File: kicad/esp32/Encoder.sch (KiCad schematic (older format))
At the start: 3 parts, among them P13 ENC_Host, P14 ENC_Slave, U11 AS5145

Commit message: 自動配線成功
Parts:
- renumbered P13 to P12, P14 to P13
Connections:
- net +3V3: now also P12.1 (P1); no longer P12.4 (P4)
- net CSn: now also P12.5 (P5); no longer P12.3 (P3)
- net GND: now also P12.6 (P6); no longer P12.5 (P5)
- net MISO: now also P12.4 (P4); no longer P12.1 (P1)
- net MOSI: now also P12.3 (P3); no longer P12.6 (P6)
- net s_3.3V: now also P13.1 (P1); no longer P13.4 (P4)
- net s_CSn: now also P13.5 (P5); no longer P13.3 (P3)
- net s_MISO: now also P13.4 (P4); no longer P13.1 (P1)
- net s_MOSI: now also P13.3 (P3); no longer P13.6 (P6)
- net s_VSS: now also P13.6 (P6); no longer P13.5 (P5)
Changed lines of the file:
@@
 $Descr A4 11693 8268
 encoding utf-8
-Sheet 10 13
+Sheet 10 14
 Title ""
 Date ""
@@
 $EndComp
 $Comp
-L CONN_01X06 P14
+L CONN_01X06 P13
 U 1 1 589E8902
 P 5800 2350
-AR Path="/589E8312/589E8902" Ref="P14"  Part="1"
-AR Path="/589F1140/589E8902" Ref="P16"  Part="1"
-F 0 "P14" H 5800 2700 50  0000 C CNN
+AR Path="/589E8312/589E8902" Ref="P13"  Part="1"
+AR Path="/589F1140/589E8902" Ref="P15"  Part="1"
+F 0 "P13" H 5800 2700 50  0000 C CNN
 F 1 "ENC_Slave" V 5900 2350 50  0000 C CNN
 F 2 "mouse:STAND_AS_SLAVE" H 5800 2350 50  0001 C CNN
@@
 	-1   0    0    -1
 $EndComp
+Text Label 6100 2100 0    60   ~ 0
+s_3.3V
+Text Label 6100 2600 0    60   ~ 0
+s_VSS
+Text Label 6100 2300 0    60   ~ 0
+s_MOSI
 Text Label 6100 2400 0    60   ~ 0
-s_3.3V
+s_MISO
 Text Label 6100 2500 0    60   ~ 0
-s_VSS
-Text Label 6100 2600 0    60   ~ 0
-s_MOSI
-Text Label 6100 2100 0    60   ~ 0
-s_MISO
-Text Label 6100 2300 0    60   ~ 0
 s_CSn
 Text Label 6100 2200 0    60   ~ 0
@@
 NoConn ~ 4900 3700
 Wire Wire Line
-	6000 2400 6700 2400
+	6000 2100 6700 2100
 Wire Wire Line
-	6000 2500 6700 2500
+	6000 2600 6700 2600
+Wire Wire Line
+	6100 2300 6000 2300
+Wire Wire Line
+	6000 2500 6100 2500
 Wire Wire Line
 	6100 2200 6000 2200
 Wire Wire Line
-	6000 2600 6100 2600
-Wire Wire Line
-	6100 2100 6000 2100
-Wire Wire Line
-	6000 2300 6100 2300
+	6000 2400 6100 2400
 Text Label 6400 3200 0    60   ~ 0
 s_3.3V
@@
 	6400 3700 6300 3700
 $Comp
-L CONN_01X06 P13
+L CONN_01X06 P12
 U 1 1 589E9420
 P 5400 2350
-AR Path="/589E8312/589E9420" Ref="P13"  Part="1"
-AR Path="/589F1140/589E9420" Ref="P15"  Part="1"
-F 0 "P13" H 5400 2700 50  0000 C CNN
+AR Path="/589E8312/589E9420" Ref="P12"  Part="1"
+AR Path="/589F1140/589E9420" Ref="P14"  Part="1"
+F 0 "P12" H 5400 2700 50  0000 C CNN
 F 1 "ENC_Host" V 5500 2350 50  0000 C CNN
 F 2 "mouse:STAND_AS_HOST" H 5400 2350 50  0001 C CNN
@@
 $EndComp
 $Comp
-L GND #PWR059
+L GND #PWR056
 U 1 1 589E94E9
 P 5100 2700
-AR Path="/589E8312/589E94E9" Ref="#PWR059"  Part="1"
-AR Path="/589F1140/589E94E9" Ref="#PWR063"  Part="1"
-F 0 "#PWR063" H 5100 2450 50  0001 C CNN
+AR Path="/589E8312/589E94E9" Ref="#PWR056"  Part="1"
+AR Path="/589F1140/589E94E9" Ref="#PWR060"  Part="1"
+F 0 "#PWR060" H 5100 2450 50  0001 C CNN
 F 1 "GND" H 5100 2550 50  0000 C CNN
 F 2 "" H 5100 2700 50  0000 C CNN
@@
 Text HLabel 5000 2200 0    60   Input ~ 0
 SCLK
-Text HLabel 5000 2600 0    60   Input ~ 0
+Text HLabel 5000 2300 0    60   Input ~ 0
 MOSI
-Text HLabel 5000 2100 0    60   Input ~ 0
+Text HLabel 5000 2400 0    60   Input ~ 0
 MISO
-Text HLabel 5000 2300 0    60   Input ~ 0
+Text HLabel 5000 2500 0    60   Input ~ 0
 CSn
+Wire Wire Line
+	5000 2300 5200 2300
 Wire Wire Line
 	5000 2200 5200 2200
 Wire Wire Line
-	5000 2100 5200 2100
-Wire Wire Line
-	5200 2300 5000 2300
+	5200 2400 5000 2400
 $Comp
-L PWR_FLAG #FLG060
+L PWR_FLAG #FLG057
 U 1 1 58CB39A3
-P 6700 2400
-AR Path="/589E8312/58CB39A3" Ref="#FLG060"  Part="1"
-AR Path="/589F1140/58CB39A3" Ref="#FLG064"  Part="1"
-F 0 "#FLG064" H 6700 2495 50  0001 C CNN
-F 1 "PWR_FLAG" H 6700 2580 50  0000 C CNN
-F 2 "" H 6700 2400 50  0000 C CNN
-F 3 "" H 6700 2400 50  0000 C CNN
-	1    6700 2400
+P 6700 2100
+AR Path="/589E8312/58CB39A3" Ref="#FLG057"  Part="1"
+AR Path="/589F1140/58CB39A3" Ref="#FLG061"  Part="1"
+F 0 "#FLG061" H 6700 2195 50  0001 C CNN
+F 1 "PWR_FLAG" H 6700 2280 50  0000 C CNN
+F 2 "" H 6700 2100 50  0000 C CNN
+F 3 "" H 6700 2100 50  0000 C CNN
+	1    6700 2100
 	1    0    0    -1
 $EndComp
 $Comp
-L PWR_FLAG #FLG061
+L PWR_FLAG #FLG058
 U 1 1 58CB39EE
-P 6700 2500
-AR Path="/589E8312/58CB39EE" Ref="#FLG061"  Part="1"
-AR Path="/589F1140/58CB39EE" Ref="#FLG065"  Part="1"
-F 0 "#FLG065" H 6700 2595 50  0001 C CNN
-F 1 "PWR_FLAG" H 6700 2680 50  0000 C CNN
-F 2 "" H 6700 2500 50  0000 C CNN
-F 3 "" H 6700 2500 50  0000 C CNN
-	1    6700 2500
+P 6700 2600
+AR Path="/589E8312/58CB39EE" Ref="#FLG058"  Part="1"
+AR Path="/589F1140/58CB39EE" Ref="#FLG062"  Part="1"
+F 0 "#FLG062" H 6700 2695 50  0001 C CNN
+F 1 "PWR_FLAG" H 6700 2780 50  0000 C CNN
+F 2 "" H 6700 2600 50  0000 C CNN
+F 3 "" H 6700 2600 50  0000 C CNN
+	1    6700 2600
 	-1   0    0    1
 $EndComp
@@
 	6400 3300 6300 3300
 $Comp
-L +3.3V #PWR062
+L +3.3V #PWR059
 U 1 1 589CCACF
 P 5100 2000
-AR Path="/589E8312/589CCACF" Ref="#PWR062"  Part="1"
-AR Path="/589F1140/589CCACF" Ref="#PWR066"  Part="1"
-F 0 "#PWR066" H 5100 1850 50  0001 C CNN
+AR Path="/589E8312/589CCACF" Ref="#PWR059"  Part="1"
+AR Path="/589F1140/589CCACF" Ref="#PWR063"  Part="1"
+F 0 "#PWR063" H 5100 1850 50  0001 C CNN
 F 1 "+3.3V" H 5100 2140 50  0000 C CNN
 F 2 "" H 5100 2000 50  0000 C CNN
@@
 $EndComp
 Wire Wire Line
-	5000 2600 5200 2600
+	5000 2500 5200 2500
 Wire Wire Line
-	5200 2400 5100 2400
+	5200 2100 5100 2100
 Wire Wire Line
-	5100 2400 5100 2000
+	5100 2100 5100 2000
 Wire Wire Line
-	5200 2500 5100 2500
+	5100 2700 5100 2600
 Wire Wire Line
-	5100 2500 5100 2700
+	5100 2600 5200 2600
 $EndSCHEMATC

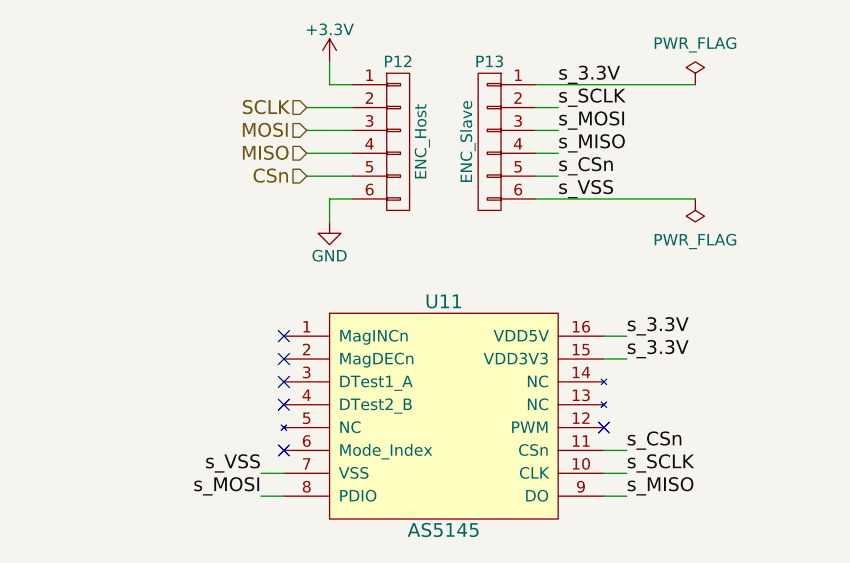
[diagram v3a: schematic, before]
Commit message: 2輪の基板を作成
部品を配置
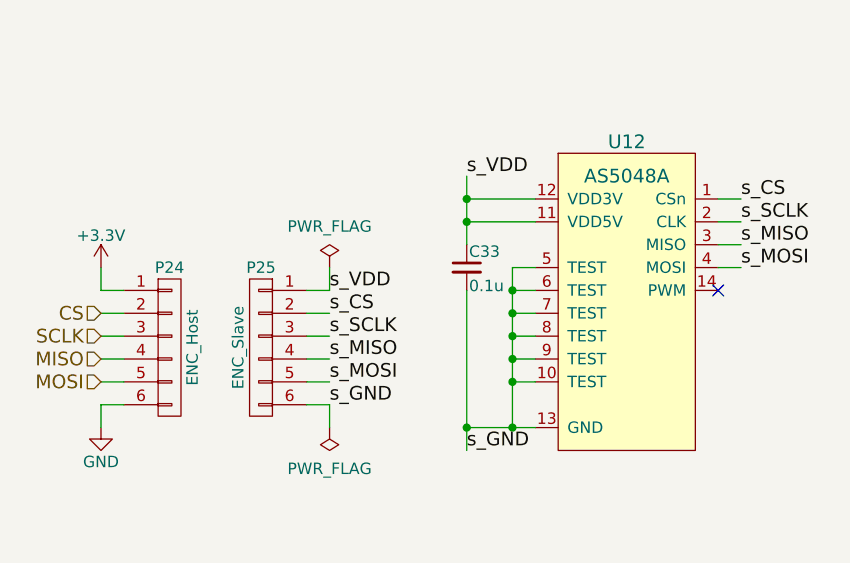
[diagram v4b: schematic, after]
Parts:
- removed P12: ENC_Host, mouse:STAND_AS_HOST, symbol CONN_01X06
- removed P13: ENC_Slave, mouse:STAND_AS_SLAVE, symbol CONN_01X06
- removed U11: AS5145, Housings_SSOP:SSOP-16_5.3x6.2mm_Pitch0.65mm, symbol AS5145
- added C26: 0.1u, Capacitors_SMD:C_0201, symbol C_Small
- added P19: ENC_Host, mouse:STAND_AS_HOST, symbol CONN_01X06
- added P20: ENC_Slave, mouse:STAND_AS_SLAVE, symbol CONN_01X06
- added U8: AS5048A, mouse:TSSOP-14_4.4x5mm_Pitch0.65mm, symbol AS5048A
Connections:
- net +3V3: now also P19.1 (P1)
- net GND: now also P19.6 (P6)
- net MISO: now also P19.4 (P4)
- net MOSI: now also P19.5 (P5)
- net SCLK: now also P19.3 (P3)
- net s_MISO: now also P20.4 (P4), U8.3 (MISO)
- net s_MOSI: now also P20.5 (P5), U8.4 (MOSI)
- net s_SCLK: now also P20.3 (P3), U8.2 (CLK)
- new net CS: P19.2 (P2)
- new net s_CS: P20.2 (P2), U8.1 (CSn)
- new net s_GND: C26.2, P20.6 (P6), U8.10 (TEST), U8.13 (GND), U8.5 (TEST), U8.6 (TEST), U8.7 (TEST), U8.8 (TEST), U8.9 (TEST)
- new net s_VDD: C26.1, P20.1 (P1), U8.11 (VDD5V), U8.12 (VDD3V)
- no-connect marks 6 -> 1
